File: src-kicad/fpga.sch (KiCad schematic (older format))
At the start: 22 parts, among them U1 iCE40HX1K-TQ144

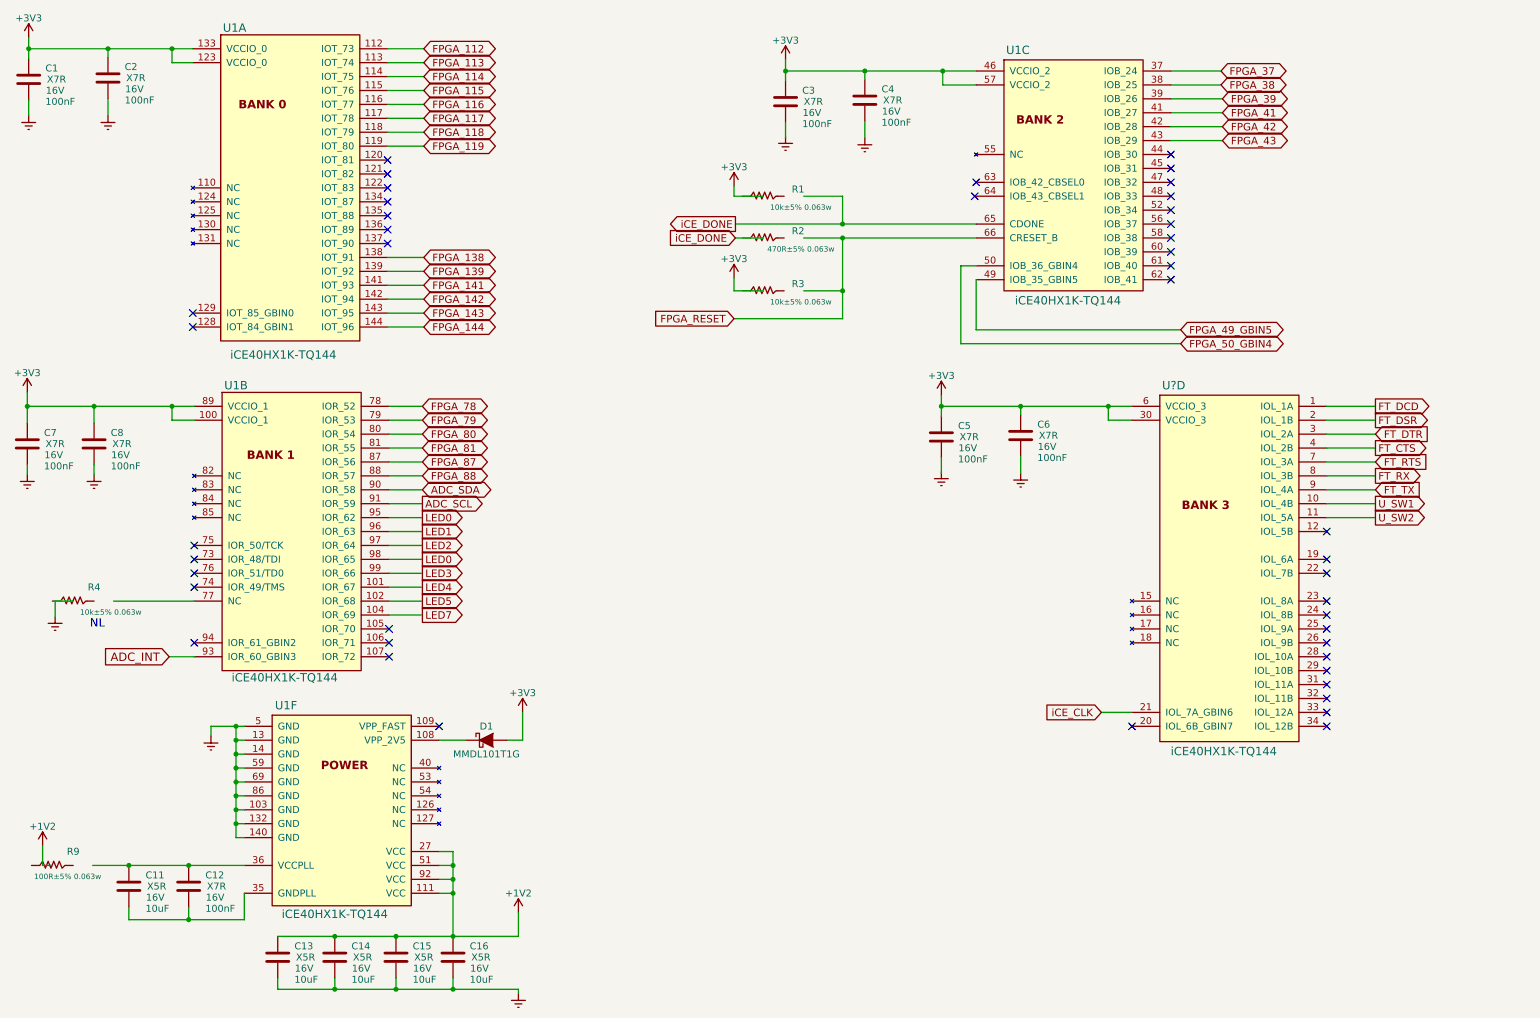
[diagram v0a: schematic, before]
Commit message: Kicad migration: fpga sheet finished (not double checked yet)
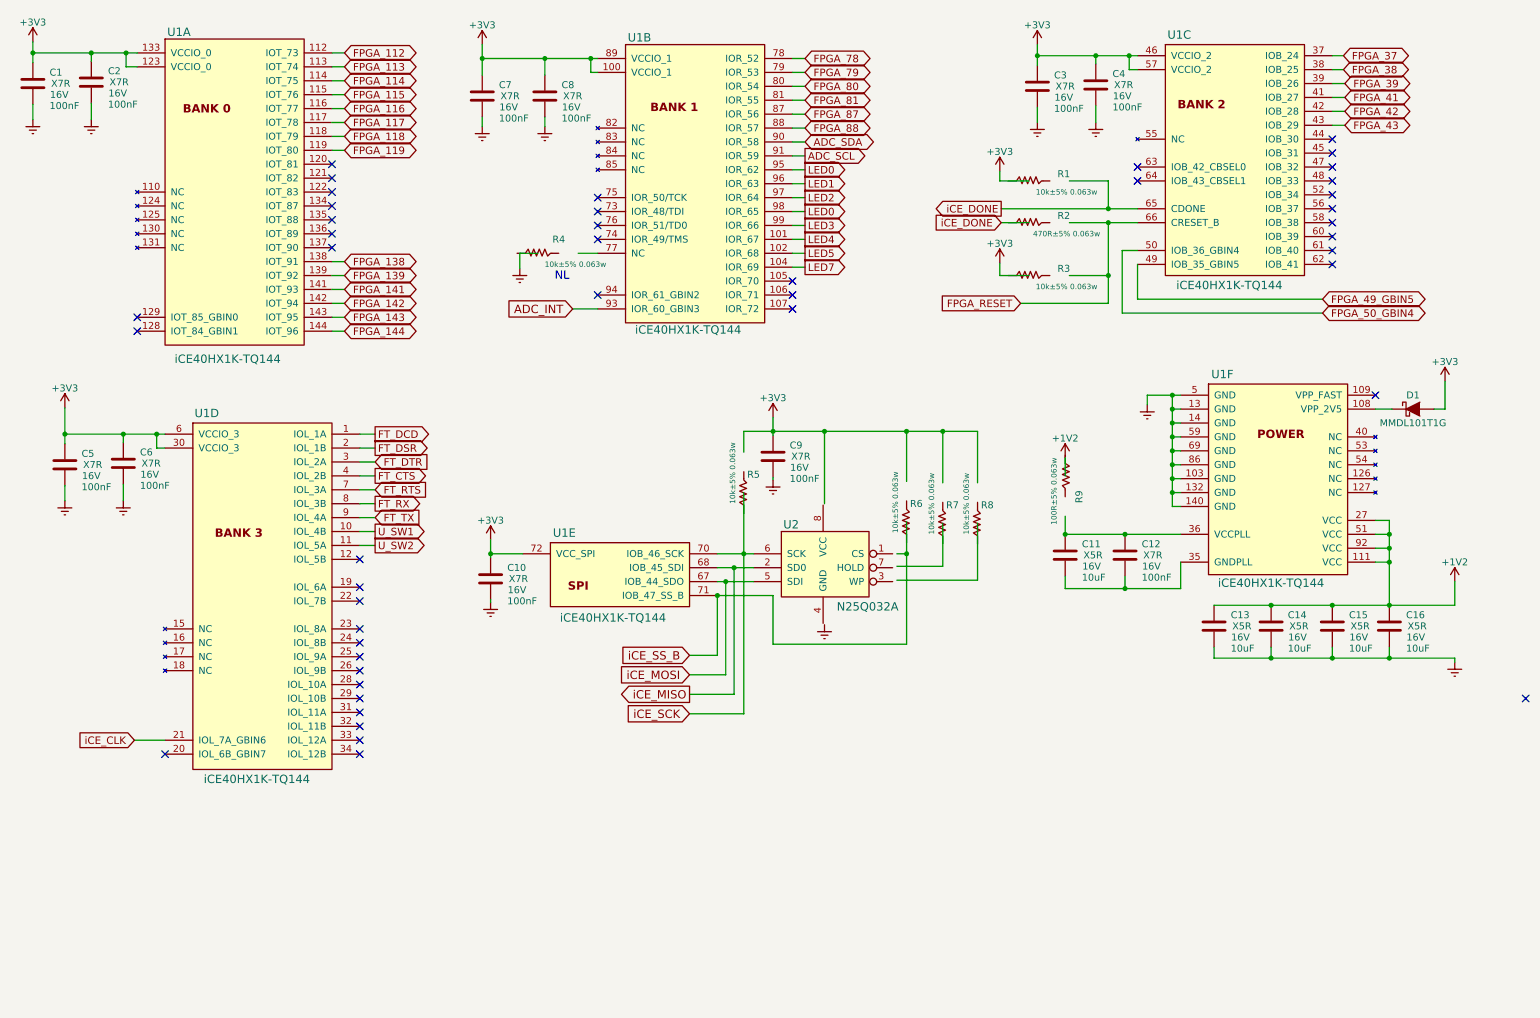
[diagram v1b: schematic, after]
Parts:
- added C10, C9: 100nF, symbol C
- added R5, R6, R7, R8: 10k±5% 0.063w, symbol R
- added unit 5 of U1
- added U2: N25Q032A, symbol N25Q032A
- gave numbers to parts that had none: 1
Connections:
- net labels added: iCE_MISO, iCE_MOSI, iCE_SCK, iCE_SS_B
- wire segments 129 -> 160
- no-connect marks 44 -> 45
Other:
- moved on the sheet: C1, C11, C12, C13, C14, C15, C16, C2, C3, C4, C5, C6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

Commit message: Kicad migration: arduino-sockets initial commit
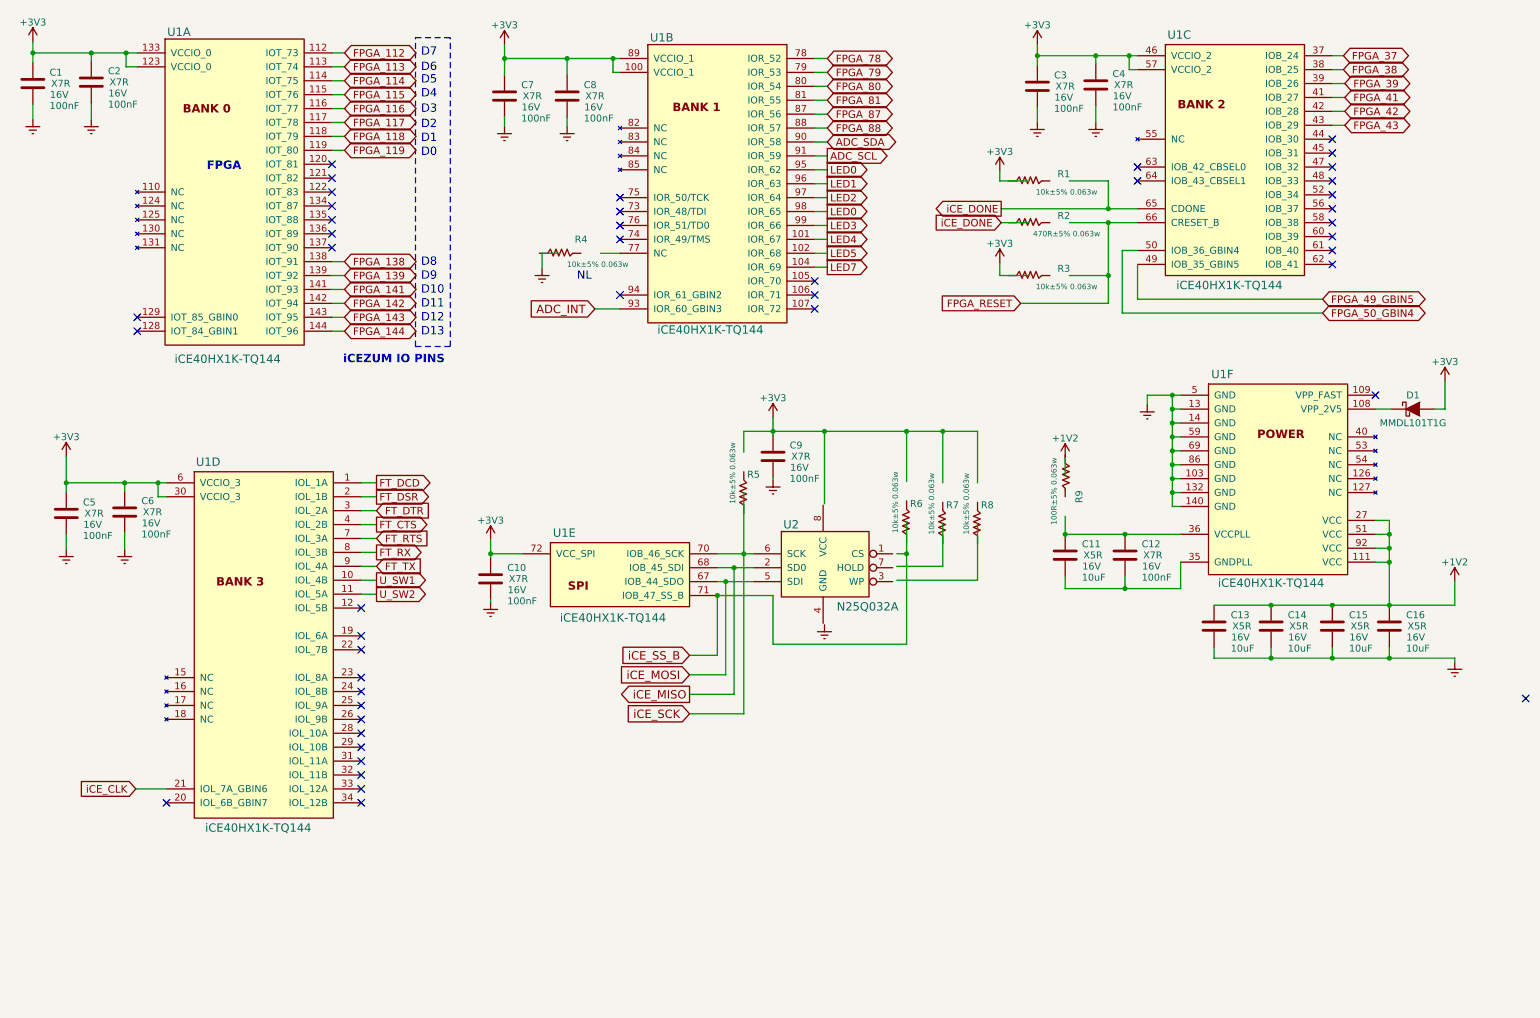
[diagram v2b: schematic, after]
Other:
- note added: "D0"
- note added: "D1"
- note added: "D10"
- note added: "D11"
- note added: "D12"
- note added: "D13"
- note added: "D2"
- note added: "D3"
- note added: "D4"
- note added: "D5"
- note added: "D6"
- note added: "D7"
- note added: "D8"
- note added: "D9"
- note added: "FPGA"
- note added: "iCEZUM IO PINS"
- moved on the sheet: C5, C6, C7, C8, R4, U1B, U1D

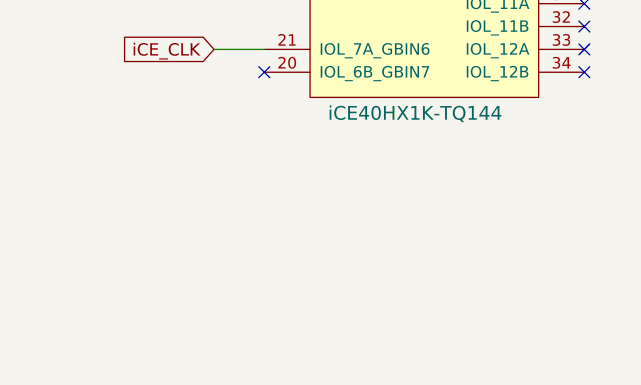
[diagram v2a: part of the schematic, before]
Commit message: Kicad migration: TXB0108 Level translator added to the library
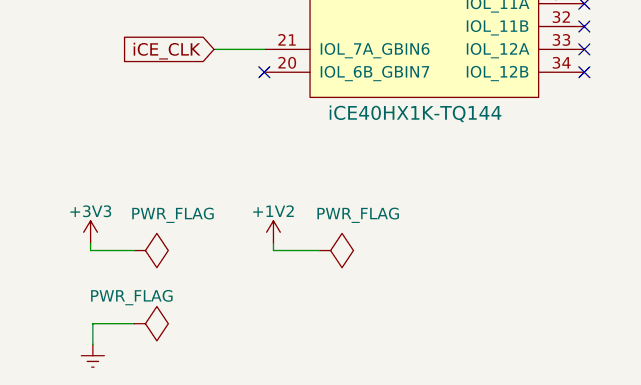
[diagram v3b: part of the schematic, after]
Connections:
- wire segments 160 -> 166
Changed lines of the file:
@@
 EESchema Schematic File Version 2
 LIBS:icezum
+LIBS:power
 LIBS:icezum-cache
 EELAYER 25 0
@@
 Text Notes 2940 3100 0    60   ~ 12
 iCEZUM IO PINS
+$Comp
+L PWR_FLAG #FLG026
+U 1 1 574561BA
+P 1100 7030
+F 0 "#FLG026" H 1100 7125 50  0001 C CNN
+F 1 "PWR_FLAG" V 940 7200 50  0000 C CNN
+F 2 "" H 1100 7030 50  0000 C CNN
+F 3 "" H 1100 7030 50  0000 C CNN
+	1    1100 7030
+	0    1    1    0
+$EndComp
+$Comp
+L +3V3 #PWR027
+U 1 1 574563BB
+P 910 7000
+F 0 "#PWR027" H 910 6850 50  0001 C CNN
+F 1 "+3V3" H 910 7140 50  0000 C CNN
+F 2 "" H 910 7000 50  0000 C CNN
+F 3 "" H 910 7000 50  0000 C CNN
+	1    910  7000
+	1    0    0    -1
+$EndComp
+Wire Wire Line
+	910  7030 910  7000
+Wire Wire Line
+	1100 7030 910  7030
+$Comp
+L GNDREF #PWR028
+U 1 1 57456DF0
+P 920 7440
+F 0 "#PWR028" H 920 7190 50  0001 C CNN
+F 1 "GNDREF" H 920 7290 50  0001 C CNN
+F 2 "" H 920 7440 50  0000 C CNN
+F 3 "" H 920 7440 50  0000 C CNN
+	1    920  7440
+	1    0    0    -1
+$EndComp
+$Comp
+L PWR_FLAG #FLG029
+U 1 1 57456EC1
+P 1100 7350
+F 0 "#FLG029" H 1100 7445 50  0001 C CNN
+F 1 "PWR_FLAG" V 980 7340 50  0000 C CNN
+F 2 "" H 1100 7350 50  0000 C CNN
+F 3 "" H 1100 7350 50  0000 C CNN
+	1    1100 7350
+	0    1    1    0
+$EndComp
+Wire Wire Line
+	920  7440 920  7350
+Wire Wire Line
+	920  7350 1100 7350
+$Comp
+L +1V2 #PWR030
+U 1 1 57457646
+P 1710 7000
+F 0 "#PWR030" H 1710 6850 50  0001 C CNN
+F 1 "+1V2" H 1710 7140 50  0000 C CNN
+F 2 "" H 1710 7000 50  0000 C CNN
+F 3 "" H 1710 7000 50  0000 C CNN
+	1    1710 7000
+	1    0    0    -1
+$EndComp
+$Comp
+L PWR_FLAG #FLG031
+U 1 1 57457784
+P 1910 7030
+F 0 "#FLG031" H 1910 7125 50  0001 C CNN
+F 1 "PWR_FLAG" V 1750 7200 50  0000 C CNN
+F 2 "" H 1910 7030 50  0000 C CNN
+F 3 "" H 1910 7030 50  0000 C CNN
+	1    1910 7030
+	0    1    1    0
+$EndComp
+Wire Wire Line
+	1910 7030 1710 7030
+Wire Wire Line
+	1710 7030 1710 7000
 $EndSCHEMATC

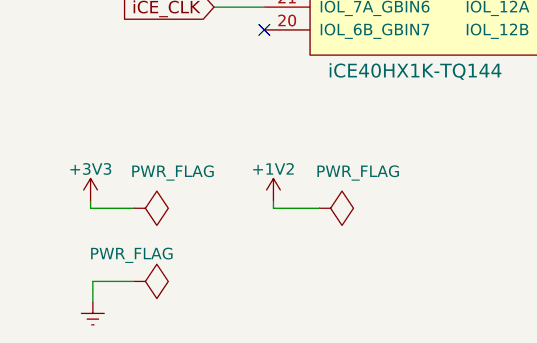
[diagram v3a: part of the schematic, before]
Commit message: Kicad migration. Power supply sheet started
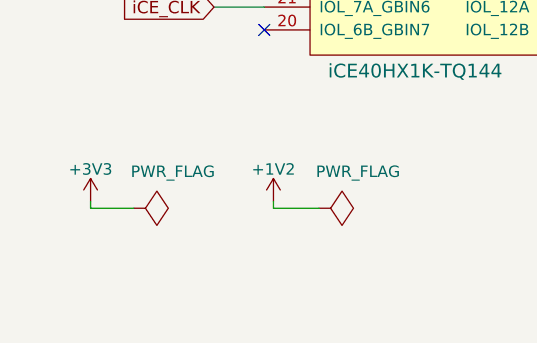
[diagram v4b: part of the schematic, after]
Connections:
- wire segments 166 -> 164
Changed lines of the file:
@@
 LIBS:icezum
 LIBS:power
+LIBS:[4]_Power_Supply-cache
+LIBS:[4]_Power_Supply-rescue
 LIBS:icezum-cache
 EELAYER 25 0
@@
 $Descr A4 11693 8268
 encoding utf-8
-Sheet 2 3
+Sheet 2 4
 Title "Icezum Alhambra"
 Date "2016-05-23"
@@
 	1100 7030 910  7030
 $Comp
-L GNDREF #PWR028
-U 1 1 57456DF0
-P 920 7440
-F 0 "#PWR028" H 920 7190 50  0001 C CNN
-F 1 "GNDREF" H 920 7290 50  0001 C CNN
-F 2 "" H 920 7440 50  0000 C CNN
-F 3 "" H 920 7440 50  0000 C CNN
-	1    920  7440
-	1    0    0    -1
-$EndComp
-$Comp
-L PWR_FLAG #FLG029
-U 1 1 57456EC1
-P 1100 7350
-F 0 "#FLG029" H 1100 7445 50  0001 C CNN
-F 1 "PWR_FLAG" V 980 7340 50  0000 C CNN
-F 2 "" H 1100 7350 50  0000 C CNN
-F 3 "" H 1100 7350 50  0000 C CNN
-	1    1100 7350
-	0    1    1    0
-$EndComp
-Wire Wire Line
-	920  7440 920  7350
-Wire Wire Line
-	920  7350 1100 7350
-$Comp
-L +1V2 #PWR030
+L +1V2 #PWR028
 U 1 1 57457646
 P 1710 7000
-F 0 "#PWR030" H 1710 6850 50  0001 C CNN
+F 0 "#PWR028" H 1710 6850 50  0001 C CNN
 F 1 "+1V2" H 1710 7140 50  0000 C CNN
 F 2 "" H 1710 7000 50  0000 C CNN
@@
 $EndComp
 $Comp
-L PWR_FLAG #FLG031
+L PWR_FLAG #FLG029
 U 1 1 57457784
 P 1910 7030
-F 0 "#FLG031" H 1910 7125 50  0001 C CNN
+F 0 "#FLG029" H 1910 7125 50  0001 C CNN
 F 1 "PWR_FLAG" V 1750 7200 50  0000 C CNN
 F 2 "" H 1910 7030 50  0000 C CNN

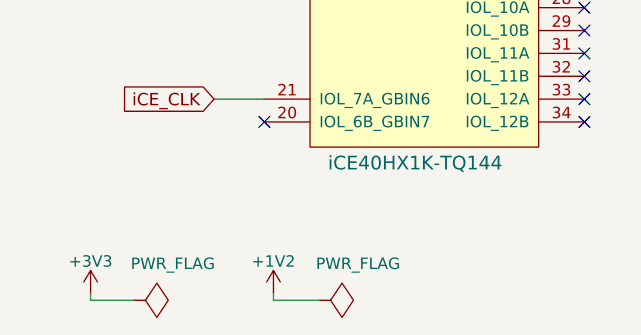
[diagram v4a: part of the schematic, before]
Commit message: Kicad migration: power supply sheet finished
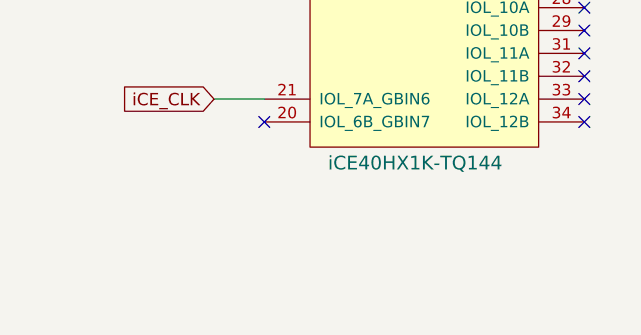
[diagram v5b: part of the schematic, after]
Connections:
- wire segments 164 -> 160
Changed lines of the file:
@@
 Text Notes 2940 3100 0    60   ~ 12
 iCEZUM IO PINS
-$Comp
-L PWR_FLAG #FLG026
-U 1 1 574561BA
-P 1100 7030
-F 0 "#FLG026" H 1100 7125 50  0001 C CNN
-F 1 "PWR_FLAG" V 940 7200 50  0000 C CNN
-F 2 "" H 1100 7030 50  0000 C CNN
-F 3 "" H 1100 7030 50  0000 C CNN
-	1    1100 7030
-	0    1    1    0
-$EndComp
-$Comp
-L +3V3 #PWR027
-U 1 1 574563BB
-P 910 7000
-F 0 "#PWR027" H 910 6850 50  0001 C CNN
-F 1 "+3V3" H 910 7140 50  0000 C CNN
-F 2 "" H 910 7000 50  0000 C CNN
-F 3 "" H 910 7000 50  0000 C CNN
-	1    910  7000
-	1    0    0    -1
-$EndComp
-Wire Wire Line
-	910  7030 910  7000
-Wire Wire Line
-	1100 7030 910  7030
-$Comp
-L +1V2 #PWR028
-U 1 1 57457646
-P 1710 7000
-F 0 "#PWR028" H 1710 6850 50  0001 C CNN
-F 1 "+1V2" H 1710 7140 50  0000 C CNN
-F 2 "" H 1710 7000 50  0000 C CNN
-F 3 "" H 1710 7000 50  0000 C CNN
-	1    1710 7000
-	1    0    0    -1
-$EndComp
-$Comp
-L PWR_FLAG #FLG029
-U 1 1 57457784
-P 1910 7030
-F 0 "#FLG029" H 1910 7125 50  0001 C CNN
-F 1 "PWR_FLAG" V 1750 7200 50  0000 C CNN
-F 2 "" H 1910 7030 50  0000 C CNN
-F 3 "" H 1910 7030 50  0000 C CNN
-	1    1910 7030
-	0    1    1    0
-$EndComp
-Wire Wire Line
-	1910 7030 1710 7030
-Wire Wire Line
-	1710 7030 1710 7000
 $EndSCHEMATC
